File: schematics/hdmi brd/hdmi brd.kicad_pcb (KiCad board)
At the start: 2 copper layers, 42.7 x 83.8 mm, 25 parts, among them J1 Conn_02x32_Odd_Even, J2 685119134923, U1 SII9022ACNU, U2 AZ1117EH-1.2TRG1

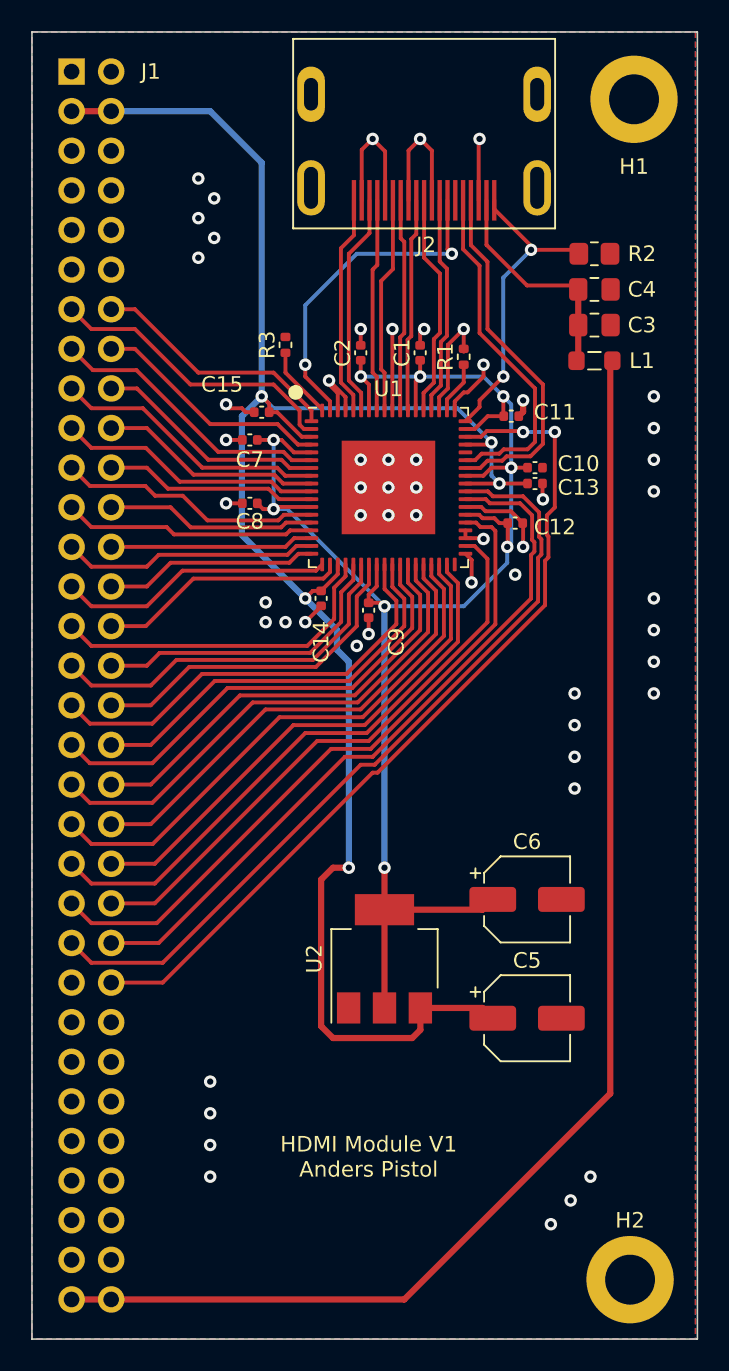
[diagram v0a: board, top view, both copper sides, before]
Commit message: Rv32: Rev 2 of HDMI board. Ordered from JLCPCB.
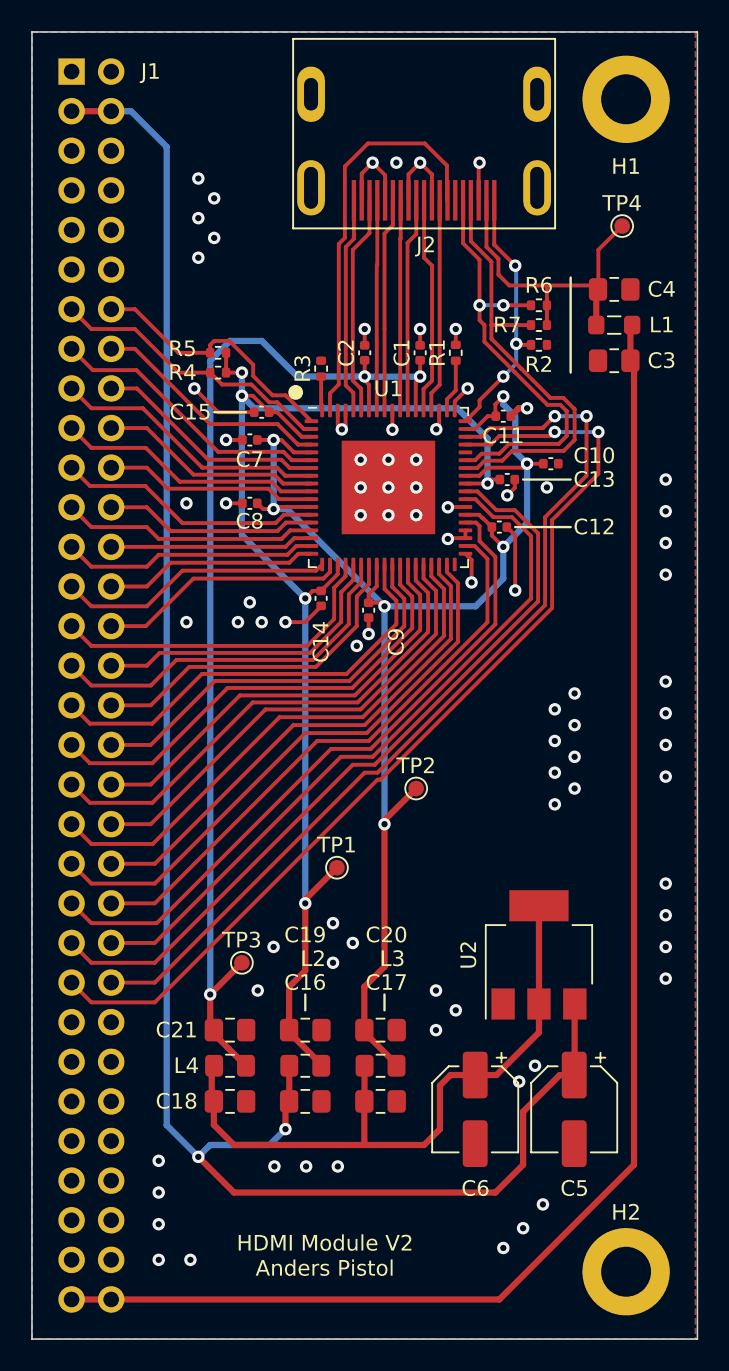
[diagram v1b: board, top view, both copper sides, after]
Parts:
- added C16: 0.1uF, Capacitor_SMD:C_0805_2012Metric_Pad1.18x1.45mm_HandSolder, F.Cu at (91.2, 114.3)
- added C17: 0.1uF, Capacitor_SMD:C_0805_2012Metric_Pad1.18x1.45mm_HandSolder, F.Cu at (96.0, 114.3)
- added C18: 0.1uF, Capacitor_SMD:C_0805_2012Metric_Pad1.18x1.45mm_HandSolder, F.Cu at (86.4, 114.3)
- added C19: 100nF, Capacitor_SMD:C_0805_2012Metric_Pad1.18x1.45mm_HandSolder, F.Cu at (91.2, 109.7)
- added C20: 100nF, Capacitor_SMD:C_0805_2012Metric_Pad1.18x1.45mm_HandSolder, F.Cu at (96.0, 109.7)
- added C21: 100nF, Capacitor_SMD:C_0805_2012Metric_Pad1.18x1.45mm_HandSolder, F.Cu at (86.4, 109.7)
- added L2: 0.022uH, Inductor_SMD:L_0805_2012Metric_Pad1.15x1.40mm_HandSolder, F.Cu at (91.2, 112.0)
- added L3: 0.022uH, Inductor_SMD:L_0805_2012Metric_Pad1.15x1.40mm_HandSolder, F.Cu at (96.0, 112.0)
- added L4: 0.022uH, Inductor_SMD:L_0805_2012Metric_Pad1.15x1.40mm_HandSolder, F.Cu at (86.4, 112.0)
- added R4: 4.7k, Resistor_SMD:R_0402_1005Metric, F.Cu at (85.6, 67.6)
- added R5: 4.7k, Resistor_SMD:R_0402_1005Metric, F.Cu at (85.6, 66.3)
- added R6: 4.7k, Resistor_SMD:R_0402_1005Metric, F.Cu at (106.2, 63.2)
- added R7: 4.7k, Resistor_SMD:R_0402_1005Metric, F.Cu at (106.2, 64.5)
- added TP1: TestPoint, TestPoint:TestPoint_Pad_D1.0mm, F.Cu at (93.2, 99.3)
- added TP2: TestPoint, TestPoint:TestPoint_Pad_D1.0mm, F.Cu at (98.3, 94.2)
- added TP3: TestPoint, TestPoint:TestPoint_Pad_D1.0mm, F.Cu at (87.1, 105.4)
- added TP4: TestPoint, TestPoint:TestPoint_Pad_D1.0mm, F.Cu at (111.5, 58.2)
- L1: value L_Small -> 0.022uH
- R2: footprint Resistor_SMD:R_0805_2012Metric_Pad1.20x1.40mm_HandSolder -> Resistor_SMD:R_0402_1005Metric
- moved C6 13.9 mm to (102.1, 114.8), turned to -90 degrees
- moved U2 9.91 mm to (106.2, 104.9)
- moved R2 6.84 mm to (106.2, 65.8)
- moved C5 6.58 mm to (108.4, 114.8), turned to -90 degrees
- moved R3 2.75 mm to (92.2, 67.3)
- moved C3 2.62 mm to (111.0, 66.8), turned to 180 degrees
- moved L1 2.62 mm to (111.0, 64.5)
- moved C13 1.80 mm to (104.1, 74.4)
- moved C4 1.27 mm to (111.0, 62.2)
- moved C12 1.05 mm to (103.6, 77.5)
- moved C10 1.05 mm to (106.9, 73.4)
- moved R1 0.57 mm to (100.8, 66.3)
- moved H2 0.57 mm to (111.8, 125.2)
- moved C11 0.51 mm to (103.9, 70.4)
- moved H1 0.51 mm to (111.8, 50.0)
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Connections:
- net /TX0+ renamed TX0+
- net /TX0- renamed TX0-
- net /TX1+ renamed TX1+
- net /TX1- renamed TX1-
- net /TX2+ renamed TX2+
- net /TX2- renamed TX2-
- net /TXC+ renamed TXC+
- net /TXC- renamed TXC-
- C1 pad 1: 1V2 -> AVCC12_1V2
- C10 pad 1: 1V2 -> CVCC12_1V2
- C11 pad 1: 1V2 -> CVCC12_1V2
- C12 pad 1: 1V2 -> CVCC12_1V2
- C13 pad 1: 3V3 -> IOVCC_3V3
- C14 pad 1: 3V3 -> IOVCC_3V3
- C15 pad 1: 3V3 -> IOVCC_3V3
- C2 pad 1: 1V2 -> AVCC12_1V2
- C3 pad 1: 5V0 -> VIN
- C7 pad 1: 1V2 -> CVCC12_1V2
- C8 pad 1: 1V2 -> CVCC12_1V2
- C9 pad 1: 1V2 -> CVCC12_1V2
- J1 pad 47: unconnected-(J1-Pad47) -> ~RESET
- U1 pad 12: 1V2 -> CVCC12_1V2
- U1 pad 21: 3V3 -> IOVCC_3V3
- U1 pad 26: 1V2 -> CVCC12_1V2
- U1 pad 3: 3V3 -> IOVCC_3V3
- U1 pad 42: 1V2 -> CVCC12_1V2
- U1 pad 46: 3V3 -> IOVCC_3V3
- U1 pad 47: 1V2 -> CVCC12_1V2
- U1 pad 5: 1V2 -> CVCC12_1V2
- U1 pad 51: 3V3 -> ~RESET
- U1 pad 53: 1V2 -> CVCC12_1V2
- U1 pad 60: 1V2 -> AVCC12_1V2
- U1 pad 66: 1V2 -> AVCC12_1V2
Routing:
- net CVCC12_1V2: track 0.00 -> 93.4 mm, vias 0 -> 7
- net IOVCC_3V3: track 0.00 -> 83.7 mm, vias 0 -> 5
- net AVCC12_1V2: track 0.00 -> 70.8 mm, vias 0 -> 3
- net 1V2: track 107.6 -> 43.0 mm, vias 9 -> 0
- net ~RESET: track 0.00 -> 63.2 mm, vias 0 -> 2
- net GND: track 62.2 -> 45.2 mm, vias 57 -> 84
- net 5V0: track 13.9 -> 21.4 mm
- net /DSCL: track 22.3 -> 28.8 mm, vias 0 -> 2
- net VIN: track 87.1 -> 93.4 mm
- net /DSDA: track 23.1 -> 28.9 mm
- net CEC_A: track 21.7 -> 26.1 mm, vias 2 -> 0
- net INT: track 55.2 -> 59.4 mm
- net /HPD: track 19.4 -> 17.1 mm, vias 2 -> 3
- net Net-(R3-Pad1): track 4.36 -> 2.20 mm
- net 3V3: track 119.3 -> 117.9 mm, vias 5 -> 2
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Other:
- board text added: "HDMI Module V2 Anders Pistol"
- board text removed: "HDMI Module V1 Anders Pistol"
